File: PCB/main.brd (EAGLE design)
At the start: 80 x 50 mm, 51 parts, among them J1 DC-005, Q1 CSD17578Q3A

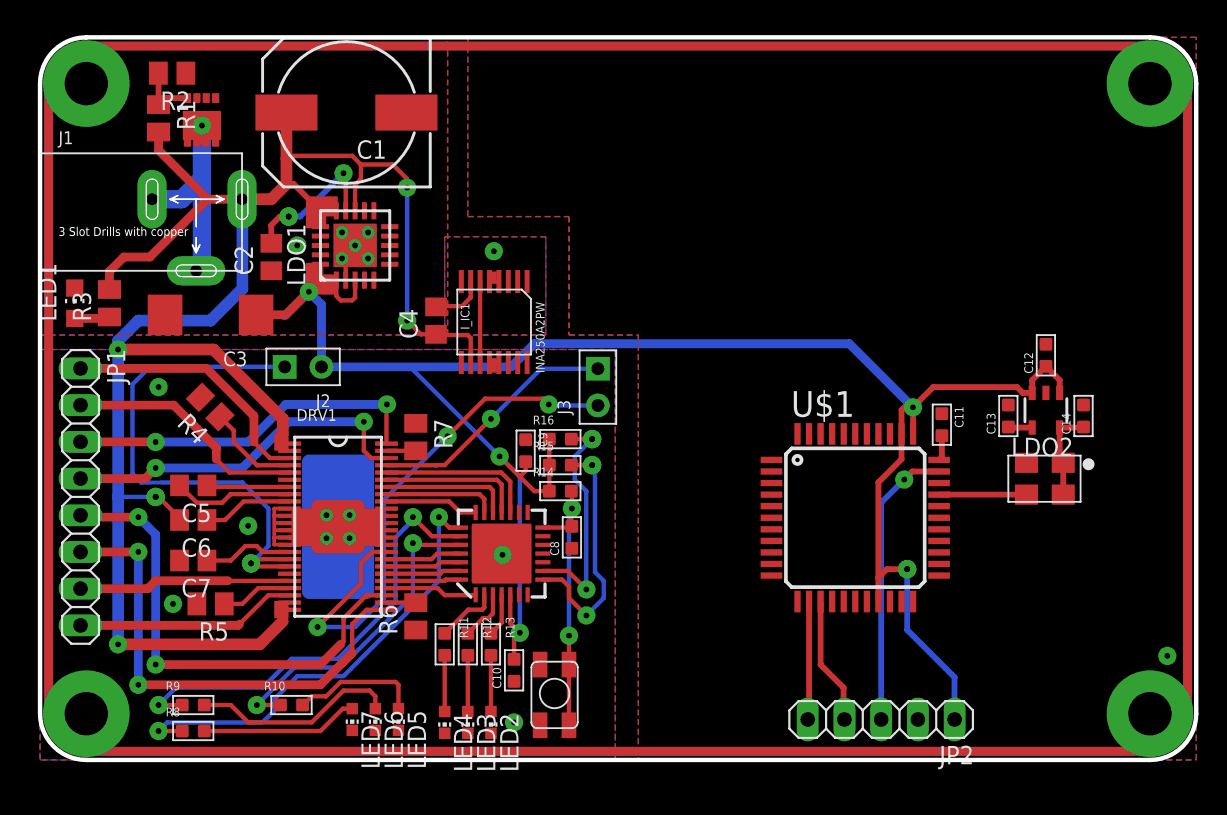
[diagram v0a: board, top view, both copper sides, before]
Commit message: Create PSoC project
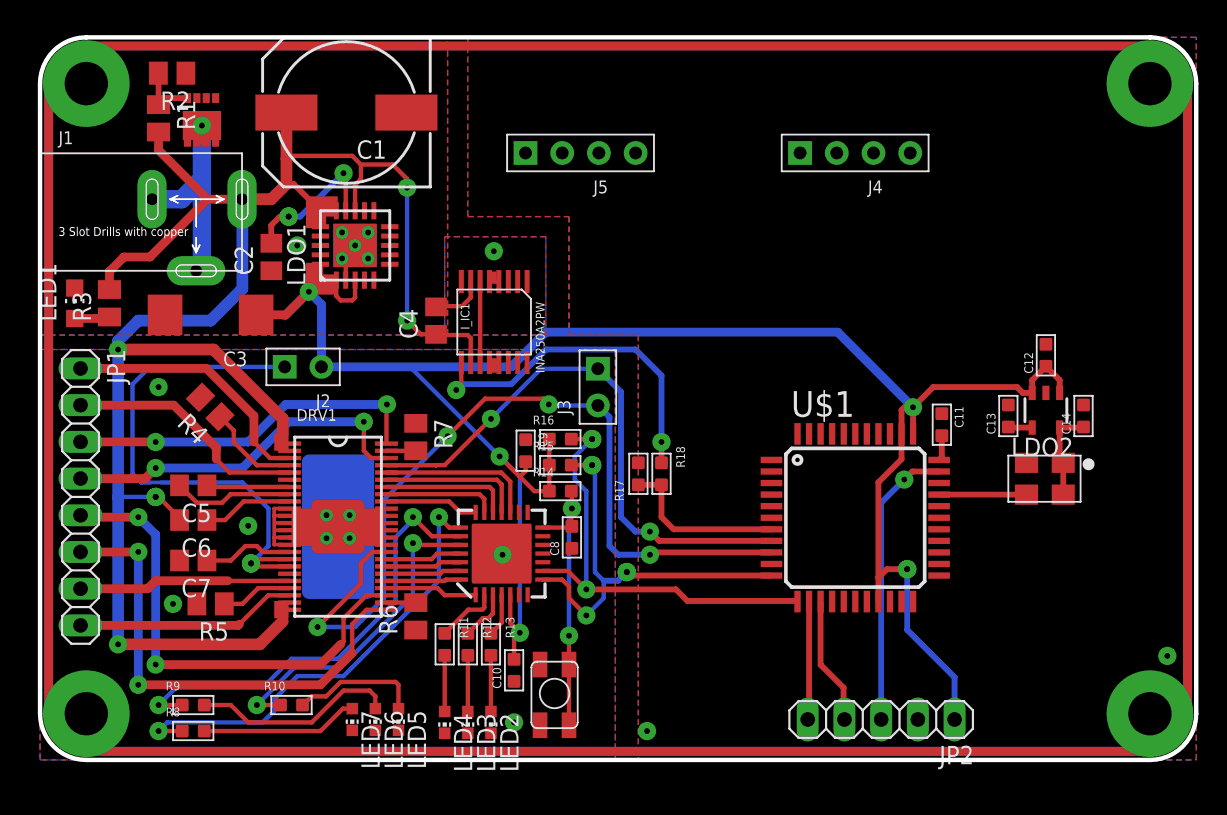
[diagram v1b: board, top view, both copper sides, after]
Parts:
- added J4, J5: 4p-2.54, Seeed-OPL-Connector:H4-2.54
- added R17, R18: (no value), My_RLC:R0603
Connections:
- new net N$60: R17.2, R18.1, U$1.7
- net CURRENT: now also R18.2
- net GND: now also J4.1, J5.1, R17.1, U$1.1, U$1.10
- net SCL: now also U$1.11
- net SDA: now also U$1.12
- net STEPAB: now also U$1.8
- net STEPCD: now also U$1.9
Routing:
- net CURRENT: track 0.00 -> 24.2 mm, vias 0 -> 2
- net STEPAB: track 17.4 -> 39.4 mm, vias 1 -> 2
- net STEPCD: track 37.9 -> 59.4 mm, vias 3 -> 4
- net SDA: track 16.2 -> 31.2 mm
- net SCL: track 17.2 -> 29.1 mm, vias 2 -> 3
- net N$60: track 0.00 -> 11.8 mm
- net +5V: track 148.6 -> 149.2 mm
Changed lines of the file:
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@@
 <?xml version="1.0" encoding="utf-8"?>
 <!DOCTYPE eagle SYSTEM "eagle.dtd">
-<eagle version="6.5.0">
+<eagle version="7.1.0">
 <drawing>
 <settings>
@@
 <layer number="56" name="wert" color="3" fill="1" visible="no" active="no"/>
 <layer number="57" name="tCAD" color="7" fill="1" visible="no" active="no"/>
-<layer number="90" name="Modules" color="5" fill="1" visible="no" active="yes"/>
+<layer number="90" name="Modules" color="5" fill="1" visible="no" active="no"/>
 <layer number="91" name="Nets" color="2" fill="1" visible="no" active="no"/>
 <layer number="92" name="Busses" color="1" fill="1" visible="no" active="no"/>
@@
 <pass name="Default">
 <param name="RoutingGrid" value="50mil"/>
+<param name="AutoGrid" value="1"/>
+<param name="Efforts" value="0"/>
+<param name="TopRouterVariant" value="1"/>
 <param name="tpViaShape" value="round"/>
 <param name="PrefDir.1" value="|"/>
@@
 <element name="C13" library="My_RLC" package="C0603" value="" x="67" y="23.8" rot="R180"/>
 <element name="C14" library="My_RLC" package="C0603" value="" x="72.2" y="23.8" rot="R180"/>
+<element name="J4" library="Seeed-OPL-Connector" package="H4-2.54" value="4p-2.54" x="56.4" y="42" rot="R90">
+<attribute name="MPN" value="F185-1104A1BSYA1" x="56.4" y="42" size="1.778" layer="27" rot="R90" display="off"/>
+</element>
+<element name="J5" library="Seeed-OPL-Connector" package="H4-2.54" value="4p-2.54" x="37.4" y="42" rot="R90">
+<attribute name="MPN" value="F185-1104A1BSYA1" x="37.4" y="42" size="1.778" layer="27" rot="R90" display="off"/>
+</element>
+<element name="R17" library="My_RLC" package="R0603" value="" x="41.4" y="19.8"/>
+<element name="R18" library="My_RLC" package="R0603" value="" x="43" y="19.8" rot="R180"/>
 </elements>
 <signals>
@@
 <via x="60.4" y="24.4" extent="1-16" drill="0.4" diameter="1.27"/>
 <wire x1="19.6" y1="27.2" x2="32.6" y2="27.2" width="0.6096" layer="16"/>
-<wire x1="32.6" y1="27.2" x2="34.2" y2="28.8" width="0.6096" layer="16"/>
-<wire x1="34.2" y1="28.8" x2="56" y2="28.8" width="0.6096" layer="16"/>
-<wire x1="56" y1="28.8" x2="60.4" y2="24.4" width="0.6096" layer="16"/>
+<wire x1="32.6" y1="27.2" x2="35" y2="29.6" width="0.6096" layer="16"/>
+<wire x1="55.2" y1="29.6" x2="60.4" y2="24.4" width="0.6096" layer="16"/>
 <wire x1="68.65" y1="25.4" x2="68" y2="25.4" width="0.4064" layer="1"/>
 <wire x1="68" y1="25.4" x2="67.6" y2="25.8" width="0.4064" layer="1"/>
 <wire x1="67.6" y1="25.8" x2="61.8" y2="25.8" width="0.4064" layer="1"/>
+<wire x1="55.2" y1="29.6" x2="35" y2="29.6" width="0.6096" layer="16"/>
 </signal>
 <signal name="N$2">
@@
 <signal name="CURRENT">
 <contactref element="I_IC1" pad="P$9"/>
+<contactref element="R18" pad="2"/>
+<wire x1="43" y1="20.562" x2="43" y2="22" width="0.4064" layer="1"/>
+<via x="43" y="22" extent="1-16" drill="0.4" diameter="1.27"/>
+<wire x1="43" y1="22" x2="43" y2="26.6" width="0.4064" layer="16"/>
+<wire x1="43" y1="26.6" x2="41.2" y2="28.4" width="0.4064" layer="16"/>
+<wire x1="41.2" y1="28.4" x2="35" y2="28.4" width="0.4064" layer="16"/>
+<wire x1="35" y1="28.4" x2="32.6" y2="26" width="0.4064" layer="16"/>
+<wire x1="32.6" y1="26" x2="29.2" y2="26" width="0.4064" layer="16"/>
+<via x="28.8" y="25.6" extent="1-16" drill="0.4" diameter="1.27"/>
+<wire x1="29.2" y1="26" x2="28.8" y2="25.6" width="0.4064" layer="16"/>
+<wire x1="29.15" y1="27.5" x2="29.15" y2="25.95" width="0.3048" layer="1"/>
+<wire x1="29.15" y1="25.95" x2="28.8" y2="25.6" width="0.3048" layer="1"/>
 </signal>
 <signal name="N$19">
@@
 <wire x1="34.79" y1="13.08" x2="36.52" y2="13.08" width="0.3048" layer="1"/>
 <wire x1="36.52" y1="13.08" x2="37.8" y2="11.8" width="0.3048" layer="1"/>
+<contactref element="U$1" pad="12"/>
+<wire x1="37.8" y1="11.8" x2="44" y2="11.8" width="0.4064" layer="1"/>
+<wire x1="44" y1="11.8" x2="44.8" y2="11" width="0.4064" layer="1"/>
+<wire x1="44.8" y1="11" x2="52.37" y2="11" width="0.4064" layer="1"/>
+<wire x1="52.37" y1="11" x2="52.41" y2="10.96" width="0.4064" layer="1"/>
 </signal>
 <signal name="SCL">
@@
 <wire x1="36.6" y1="12" x2="36.6" y2="11.2" width="0.3048" layer="1"/>
 <wire x1="36.6" y1="11.2" x2="37.8" y2="10" width="0.3048" layer="1"/>
+<contactref element="U$1" pad="11"/>
+<wire x1="39" y1="12.4" x2="40" y2="12.4" width="0.4064" layer="16"/>
+<wire x1="40" y1="12.4" x2="40.6" y2="13" width="0.4064" layer="16"/>
+<via x="40.6" y="13" extent="1-16" drill="0.4" diameter="1.27"/>
+<wire x1="40.6" y1="13" x2="40.84" y2="12.76" width="0.4064" layer="1"/>
+<wire x1="40.84" y1="12.76" x2="50.61" y2="12.76" width="0.4064" layer="1"/>
 </signal>
 <signal name="N$51">
@@
 <wire x1="31.2" y1="23.6" x2="34.67" y2="27.07" width="0.3048" layer="16"/>
 <wire x1="34.67" y1="27.07" x2="38.6" y2="27.07" width="0.3048" layer="16"/>
+<contactref element="U$1" pad="8"/>
+<wire x1="38.6" y1="27.07" x2="40.2" y2="25.47" width="0.4064" layer="16"/>
+<wire x1="40.2" y1="25.47" x2="40.2" y2="16.8" width="0.4064" layer="16"/>
+<wire x1="40.2" y1="16.8" x2="41.2" y2="15.8" width="0.4064" layer="16"/>
+<wire x1="41.2" y1="15.8" x2="42.2" y2="15.8" width="0.4064" layer="16"/>
+<via x="42.2" y="15.8" extent="1-16" drill="0.4" diameter="1.27"/>
+<wire x1="42.2" y1="15.8" x2="42.84" y2="15.16" width="0.4064" layer="1"/>
+<wire x1="42.84" y1="15.16" x2="50.61" y2="15.16" width="0.4064" layer="1"/>
 </signal>
 <signal name="STEPCD">
@@
 <wire x1="35.2" y1="24.6" x2="35.27" y2="24.53" width="0.3048" layer="16"/>
 <wire x1="35.27" y1="24.53" x2="38.6" y2="24.53" width="0.3048" layer="16"/>
+<contactref element="U$1" pad="9"/>
+<wire x1="38.6" y1="24.53" x2="39.4" y2="23.73" width="0.4064" layer="16"/>
+<wire x1="39.4" y1="23.73" x2="39.4" y2="14.8" width="0.4064" layer="16"/>
+<wire x1="39.4" y1="14.8" x2="40" y2="14.2" width="0.4064" layer="16"/>
+<wire x1="40" y1="14.2" x2="42.2" y2="14.2" width="0.4064" layer="16"/>
+<via x="42.2" y="14.2" extent="1-16" drill="0.4" diameter="1.27"/>
+<wire x1="42.2" y1="14.2" x2="42.36" y2="14.36" width="0.4064" layer="1"/>
+<wire x1="42.36" y1="14.36" x2="50.61" y2="14.36" width="0.4064" layer="1"/>
 </signal>
 <signal name="GND">
@@
 <contactref element="C14" pad="2"/>
 <via x="78" y="7.2" extent="1-16" drill="0.4" diameter="1.27"/>
+<contactref element="U$1" pad="10"/>
+<contactref element="U$1" pad="1"/>
+<contactref element="J4" pad="1"/>
+<contactref element="J5" pad="1"/>
+<contactref element="R17" pad="1"/>
+<via x="42" y="2" extent="1-16" drill="0.4" diameter="1.27"/>
 </signal>
 <signal name="N$53">
@@
 <via x="60" y="13.2" extent="1-16" drill="0.4" diameter="1.27"/>
 </signal>
+<signal name="N$59">
+<via x="40.6" y="13" extent="1-16" drill="0.4" diameter="1.27"/>
+</signal>
+<signal name="N$60">
+<contactref element="R17" pad="2"/>
+<contactref element="R18" pad="1"/>
+<contactref element="U$1" pad="7"/>
+<wire x1="41.4" y1="19.038" x2="43" y2="19.038" width="0.4064" layer="1"/>
+<wire x1="50.61" y1="15.96" x2="43.84" y2="15.96" width="0.4064" layer="1"/>
+<wire x1="43.84" y1="15.96" x2="43" y2="16.8" width="0.4064" layer="1"/>
+<wire x1="43" y1="16.8" x2="43" y2="19.038" width="0.4064" layer="1"/>
+</signal>
 </signals>

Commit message: Reroute PCB
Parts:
- removed C10, C8, C9: (no value), My_RLC:C0603
- removed J3: (no value), Seeed-OPL-Connector:H2-2.54
- removed J5: 4p-2.54, Seeed-OPL-Connector:H4-2.54
- removed R14, R15, R16, R17, R18: (no value), My_RLC:R0603
- removed U$2: MCP23017T-E/ML, I2C:QFN28(UF)
- removed U$3: MYB, Button:MYB
- added S1, S2, S3, S4: (no value), switch-omron:B3F-10XX
- moved R9 51.4 mm to (61.8, 8.20), turned to 180 degrees
- moved R8 50.0 mm to (60.2, 8.20), turned to 180 degrees
- moved R10 46.2 mm to (63.4, 8.20), turned to 180 degrees
- moved LED7 38.6 mm to (60.2, 2.80)
- moved LED5 38.6 mm to (63.4, 2.80)
- moved LED6 38.6 mm to (61.8, 2.80)
- moved LED2 37.0 mm to (68.2, 2.80)
- moved LED4 37.0 mm to (65.0, 2.80)
- moved R11 37.0 mm to (65.0, 8.20)
- moved R13 37.0 mm to (68.2, 8.20)
- moved LED3 37.0 mm to (66.6, 2.80)
- moved R12 37.0 mm to (66.6, 8.20)
- moved J4 18.0 mm to (39.2, 47.2), turned to 270 degrees
- moved C11 9.00 mm to (53.4, 23.0)
- moved C13 9.00 mm to (58.0, 23.6)
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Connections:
- removed net N$44: R13.2, U$2.4
- removed net N$45: R12.2, U$2.3
- removed net N$46: R11.2, U$2.2
- removed net N$47: R10.2, U$2.24
- removed net N$48: R9.2, U$2.23
- removed net N$49: R8.2, U$2.22
- removed net N$50: C8.2, R14.1, U$2.14, U$3.1.1, U$3.1.2
- removed net N$60: R17.2, R18.1, U$1.7
- removed net SCL: R15.1, U$1.11, U$2.8
- removed net SDA: R16.1, U$1.12, U$2.9
- removed net STEPAB: DRV1.45, J3.1, U$1.8
- removed net STEPCD: DRV1.33, J3.2, U$1.9
- new net ABDIR: DRV1.43, U$1.41
- new net ABENBLN: DRV1.42, U$1.42
- new net ABRESETN: DRV1.40, U$1.44
- new net ABSTEP: DRV1.45, U$1.39
- new net ABUSM0: DRV1.44, U$1.40
- new net ABUSM1: DRV1.41, U$1.43
- new net CDDIR: DRV1.31, U$1.4
- new net CDENBLN: DRV1.30, U$1.5
- new net CDRESETN: DRV1.28, U$1.7
- new net CDSTEP: DRV1.33, U$1.2
- new net CDUSM0: DRV1.32, U$1.3
- new net CDUSM1: DRV1.29, U$1.6
- net +24V: no longer C4.1, I_IC1.P$10
- net +3V3: now also C4.1, I_IC1.P$10
- net +5V: no longer C10.2, C9.2, R14.2, R15.2, R16.2, U$2.5
- net CURRENT: now also U$1.8; no longer R18.2
- net GND: now also LED2.C, LED3.C, LED4.C, LED5.C, LED6.C, LED7.C, S1.1, S1.2, S2.1, S2.2, S3.1, S3.2, S4.1, S4.2; no longer J5.1, R17.1
- net GNDA: no longer C10.1, C8.1, C9.1, LED2.C, LED3.C, LED4.C, LED5.C, LED6.C, LED7.C, U$2.11, U$2.12, U$2.13, U$2.6, U$3.2.1, U$3.2.2
- net N$28: now also R13.2, U$1.28; no longer DRV1.44, U$2.17
- net N$29: now also R12.2, U$1.27; no longer DRV1.43, U$2.18
- net N$30: now also R11.2, U$1.26; no longer DRV1.42, U$2.19
- net N$31: now also R10.2, U$1.25; no longer DRV1.41, U$2.20
- net N$32: now also R9.2, U$1.24; no longer DRV1.40, U$2.21
- net N$33: now also R8.2, U$1.23; no longer DRV1.32, U$2.25
- net N$34: now also S1.3, U$1.38; no longer DRV1.31, U$2.26
- net N$35: now also S2.3, U$1.37; no longer DRV1.30, U$2.27
- net N$36: now also S3.3, U$1.31; no longer DRV1.29, U$2.28
- net N$37: now also S4.4, U$1.29; no longer DRV1.28, U$2.1
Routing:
- net STEPCD: track 59.4 -> 0.00 mm, vias 4 -> 0
- net +3V3: track 6.41 -> 58.5 mm, vias 0 -> 2
- net +5V: track 149.2 -> 102.6 mm, vias 5 -> 3
- net STEPAB: track 39.4 -> 0.00 mm, vias 2 -> 0
- net N$36: track 5.16 -> 38.2 mm, vias 0 -> 1
- net N$49: track 32.0 -> 0.00 mm, vias 2 -> 0
- net SDA: track 31.2 -> 0.00 mm, vias 2 -> 0
- net N$48: track 31.2 -> 0.00 mm, vias 2 -> 0
- net SCL: track 29.1 -> 0.00 mm, vias 3 -> 0
- net ABSTEP: track 0.00 -> 28.3 mm
- net ABUSM0: track 0.00 -> 27.2 mm
- net N$37: track 6.37 -> 33.3 mm
- net ABDIR: track 0.00 -> 26.1 mm
- net ABENBLN: track 0.00 -> 25.1 mm
- net ABUSM1: track 0.00 -> 24.0 mm
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
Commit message: Bug Fix/ Final Version
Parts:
- added LED8, LED9: (no value), led:CHIP-LED0603
- added R14, R15, R17: (no value), My_RLC:R0603
- added R16: (no value), rcl:M0805
- moved J4 4.40 mm to (34.8, 47.2)
- moved R1 4.12 mm to (12.2, 43.4), turned to 0 degrees
- moved R2 3.45 mm to (12.2, 45.9)
- moved Q1 2.47 mm to (9.60, 43.4), turned to 0 degrees
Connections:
- new net N$44: J4.2, LED8.C, U$1.12
- new net N$45: J4.3, LED9.C, U$1.11
- new net N$48: R17.2, U$4.1
- new net N$49: LED9.A, R15.1
- new net N$50: LED8.A, R14.1
- net +3V3: now also R17.1; no longer C4.1, I_IC1.P$10, U$4.1
- net +5V: now also C4.1, I_IC1.P$10, J4.4, R14.2, R15.2
- net AGND: now also Q1.D1, Q1.D2, Q1.D3, Q1.D4, Q1.D5; no longer Q1.S1, Q1.S2, Q1.S3
- net GND: now also R16.2
- net GNDA: now also R16.1
- net N$1: now also Q1.S1, Q1.S2, Q1.S3; no longer Q1.D1, Q1.D2, Q1.D3, Q1.D4, Q1.D5
- net N$34: now also S1.4
- net N$35: now also S2.4
- net N$36: now also S3.4
- net N$37: now also S4.3
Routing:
- net N$44: track 0.00 -> 54.8 mm, vias 0 -> 3
- net N$45: track 0.00 -> 51.6 mm, vias 0 -> 3
- net +3V3: track 58.5 -> 15.9 mm, vias 2 -> 0
- net +5V: track 102.6 -> 133.6 mm, vias 3 -> 5
- net N$47: track 0.00 -> 17.6 mm
- net N$46: track 0.00 -> 17.6 mm
- net N$50: track 0.00 -> 13.4 mm, vias 0 -> 2
- net N$49: track 0.00 -> 12.6 mm, vias 0 -> 2
- net N$35: track 14.6 -> 21.1 mm
- net N$37: track 33.3 -> 39.8 mm
- net N$36: track 38.2 -> 44.7 mm
- net N$34: track 23.0 -> 29.5 mm
- net N$48: track 0.00 -> 4.36 mm
- net N$1: track 20.2 -> 16.6 mm
- net AGND: track 13.8 -> 16.4 mm, vias 2 -> 3
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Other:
- board text added: "A"
- board text added: "B"
- board text added: "GND"
- board text added: "Mazilyauskas"
- board text added: "RX"
- board text added: "TX"
- board text added: "VCC"
